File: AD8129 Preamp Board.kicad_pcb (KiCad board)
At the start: 2 copper layers, 50 x 42 mm, 39 parts, among them J1 ANT, J2 TUNE, J3 TRX, T1 Transformer_1P_1S, U1 AD8129, U2 L78L06_SO8

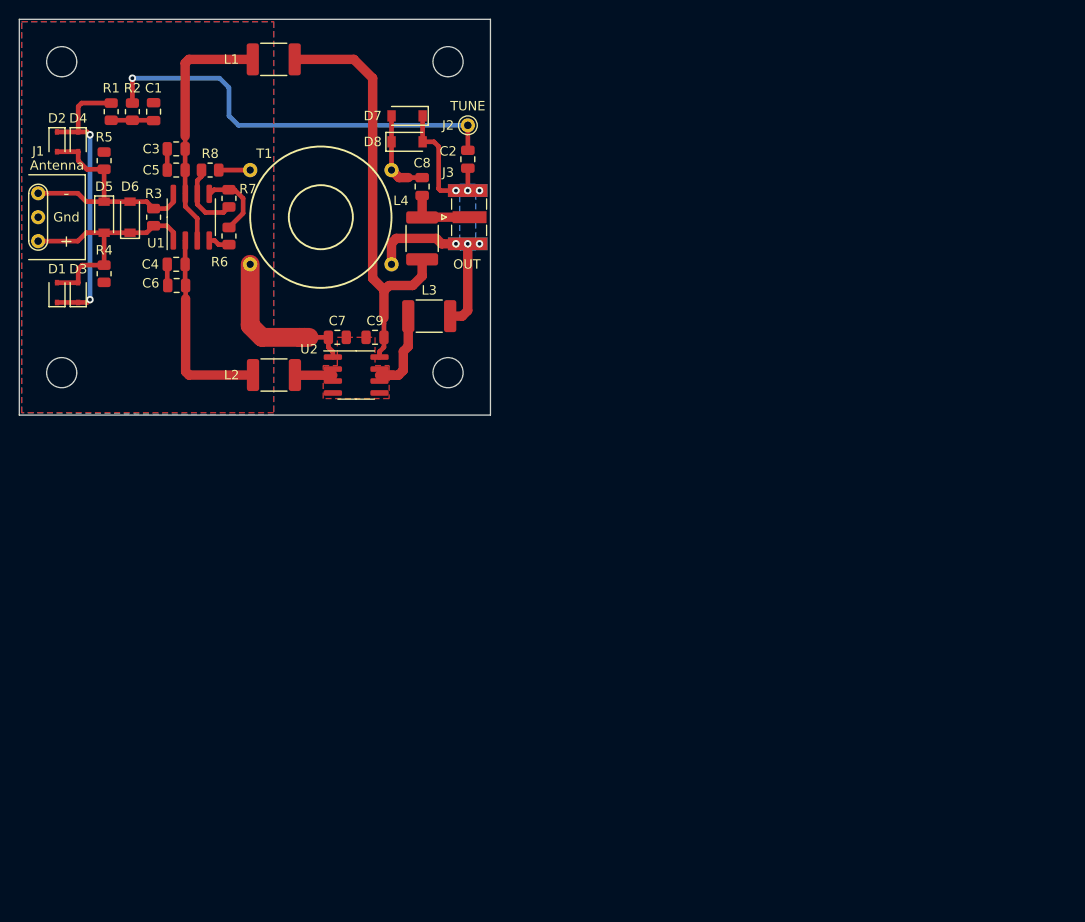
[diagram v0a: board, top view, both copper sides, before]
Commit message: FIX: board position
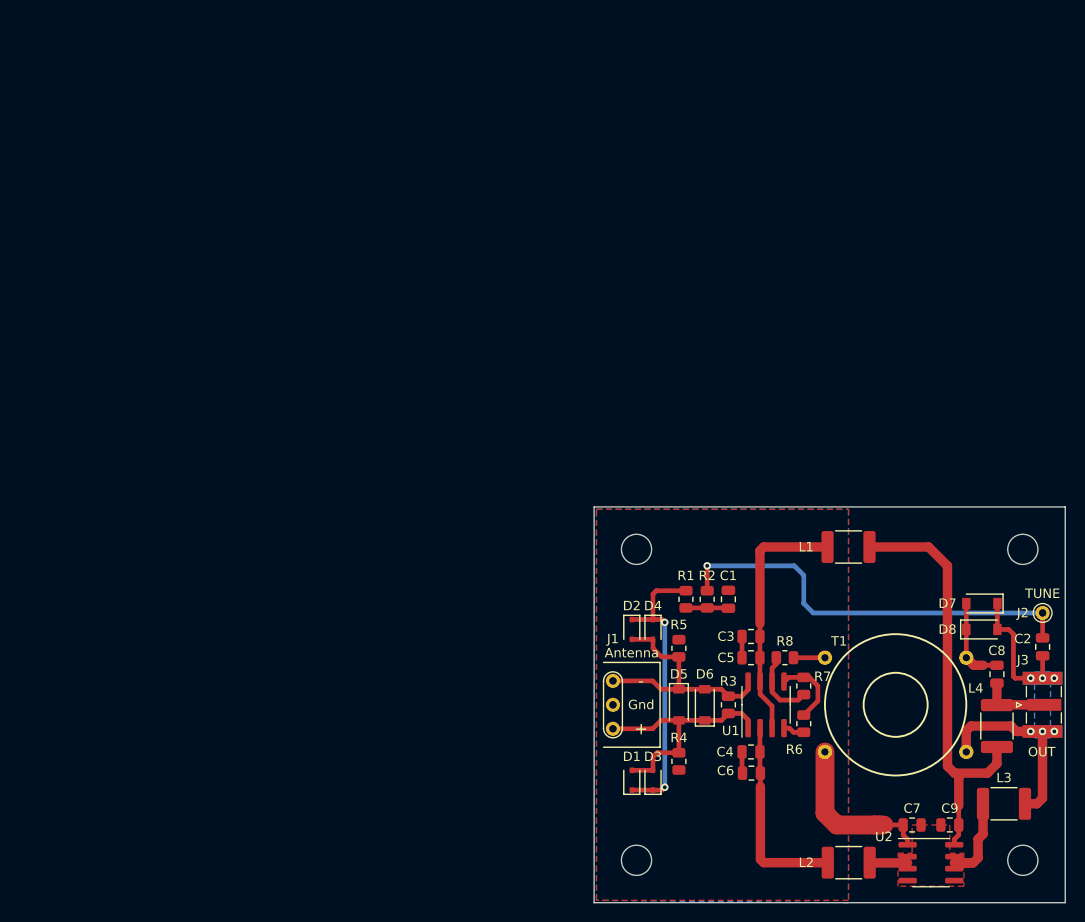
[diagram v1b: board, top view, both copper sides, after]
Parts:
- moved C1 80.0 mm to (135.2, 90.5)
- moved C2 80.0 mm to (168.6, 95.6)
- moved C3 80.0 mm to (137.7, 94.5)
- moved C4 80.0 mm to (137.7, 106.8)
- moved C5 80.0 mm to (137.7, 96.8)
- moved C6 80.0 mm to (137.7, 109.0)
- moved C7 80.0 mm to (154.8, 114.5)
- moved C8 80.0 mm to (163.8, 98.5)
- moved C9 80.0 mm to (158.8, 114.5)
- moved D1 80.0 mm to (125.0, 109.8)
- moved D2 80.0 mm to (125.0, 93.8)
- moved D3 80.0 mm to (127.2, 109.8)
- moved D4 80.0 mm to (127.2, 93.8)
- moved D5 80.0 mm to (130.0, 101.8)
- moved D6 80.0 mm to (132.8, 101.8)
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
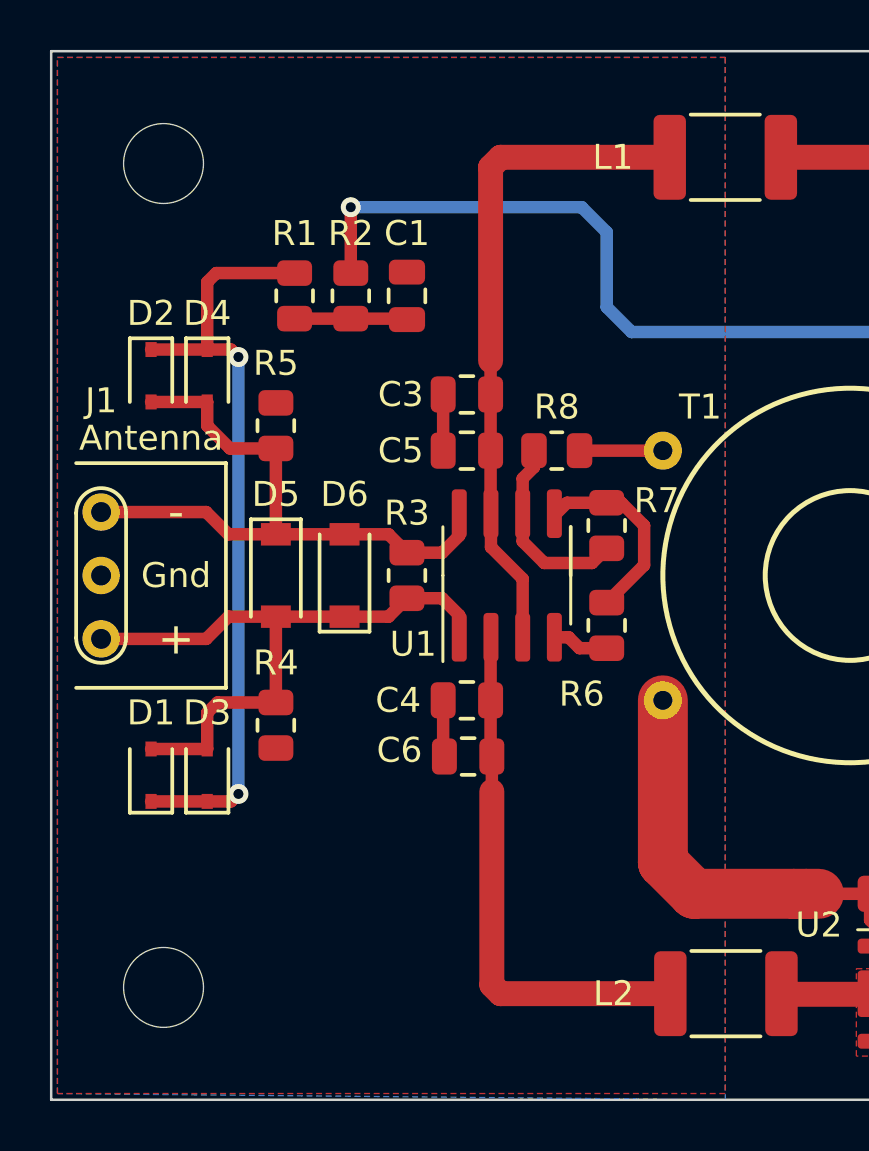
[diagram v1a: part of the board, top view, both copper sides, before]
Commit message: ADD: via stitching
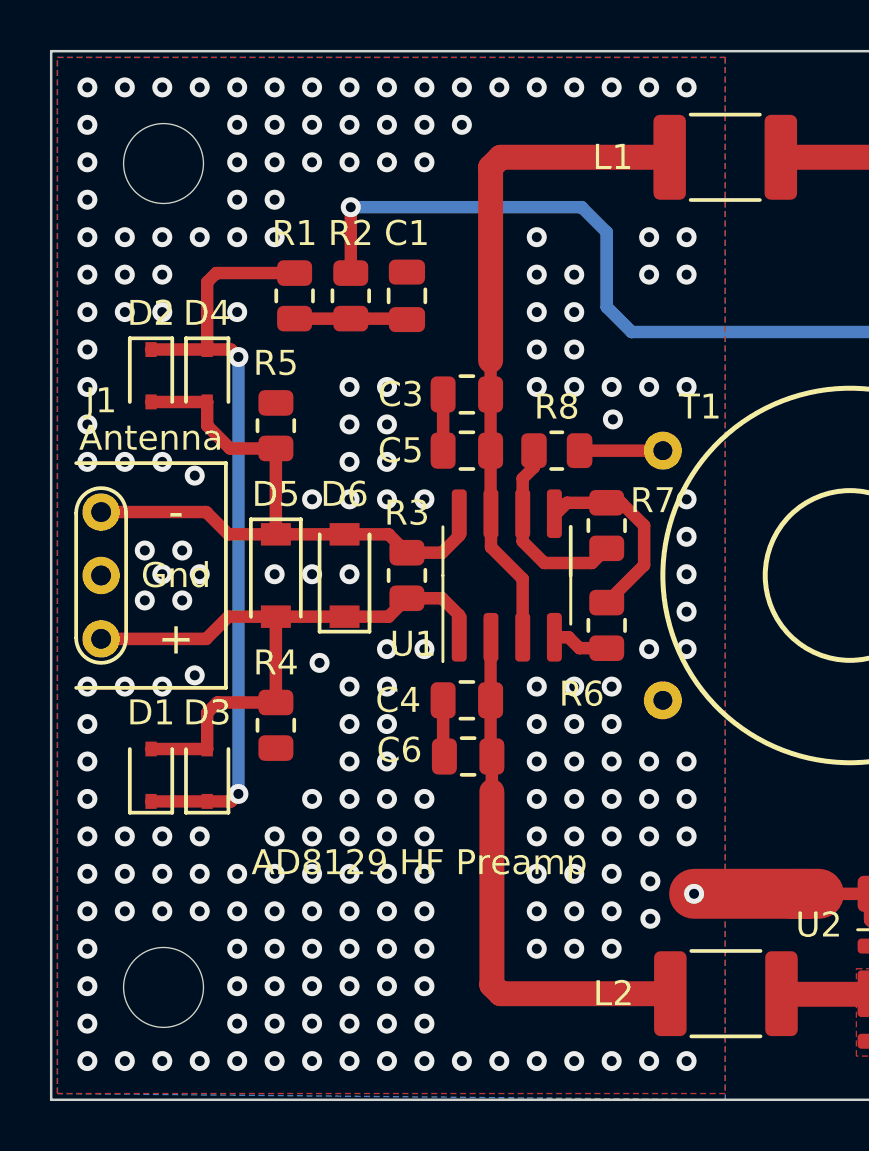
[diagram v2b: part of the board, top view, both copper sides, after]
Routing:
- net GND: track 24.4 -> 16.1 mm, vias 0 -> 217
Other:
- board text added: "AD8129 HF Preamp"

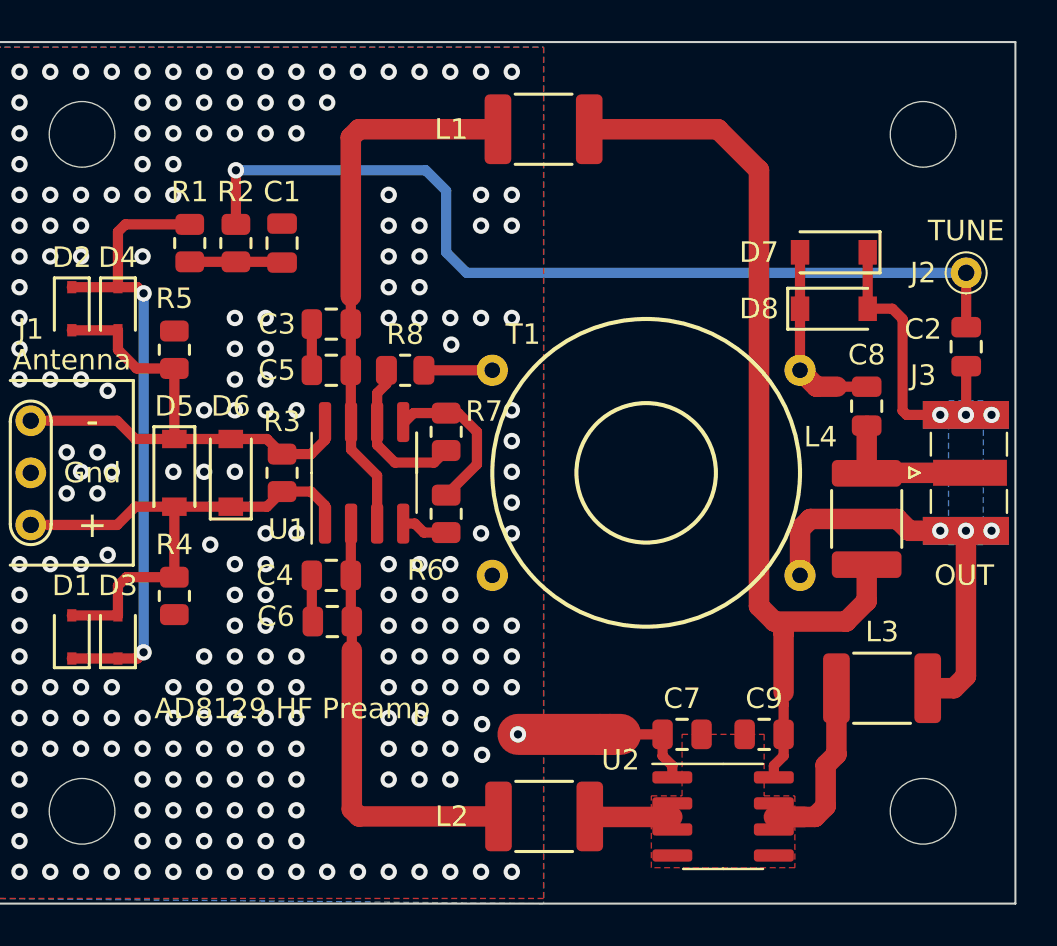
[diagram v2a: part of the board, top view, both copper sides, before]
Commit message: FIX: make burried vias, board info
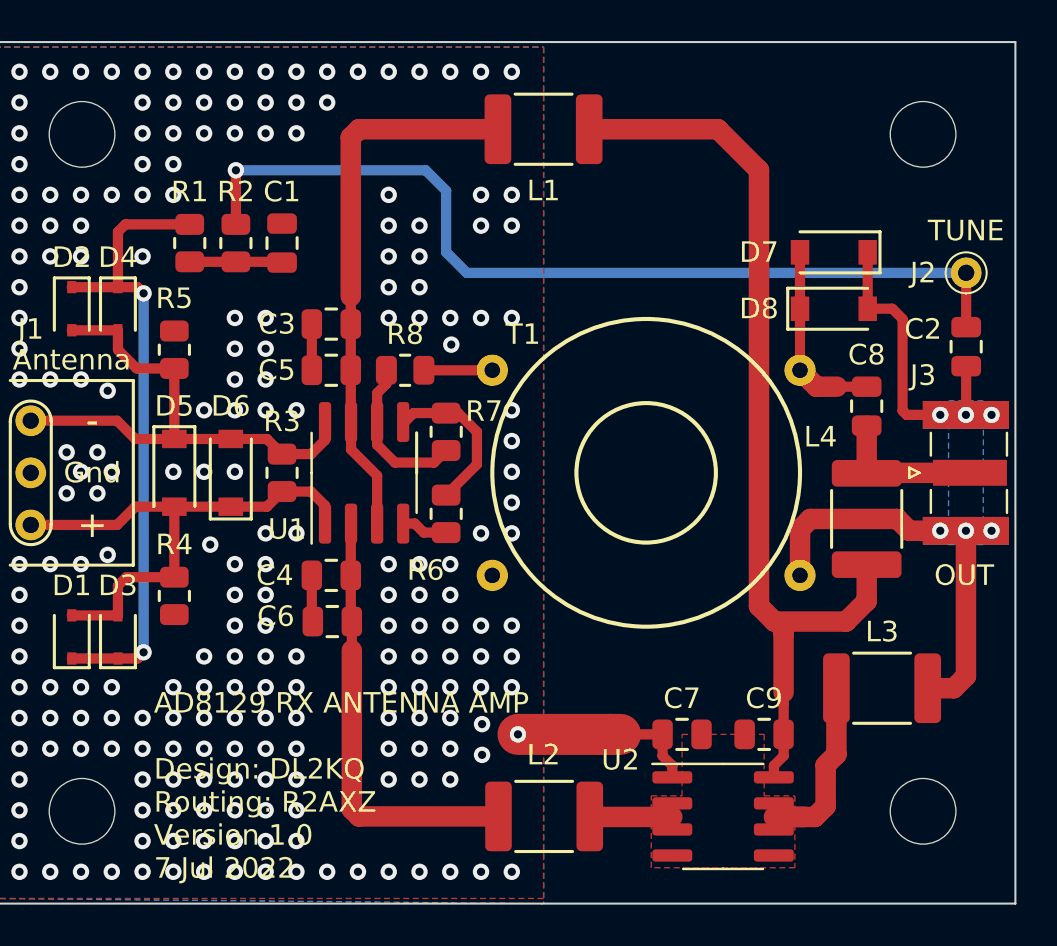
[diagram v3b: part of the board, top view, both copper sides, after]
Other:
- board text added: "AD8129 RX ANTENNA AMP Design: DL2KQ Routing: R2AXZ Version 1.0 7 Jul 2022"
- board text removed: "AD8129 HF Preamp"

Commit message: ADD: v1 final touch
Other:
- board text added: "Check out schematics for the input stage options."
- board text added: "Gain = 1 + R7/R6 Adjust R4, R5 for a desired Q, match within 0.1%."
- board text added: "Match R3 to the antenna impedance."
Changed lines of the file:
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@@
     (property "Sheetname" "")
     (attr smd)
-    (fp_text reference "L1" (at 0 3 180) (layer "F.SilkS")
+    (fp_text reference "L1" (at -4.25 1 180) (layer "F.SilkS")
       (effects (font (size 1 1) (thickness 0.15)))
     )
@@
     (property "Sheetname" "")
     (attr smd)
-    (fp_text reference "L2" (at 0.025 3 180) (layer "F.SilkS")
+    (fp_text reference "L2" (at 4.275 1 180) (layer "F.SilkS")
       (effects (font (size 1 1) (thickness 0.15)))
     )
@@
     (effects (font (size 1 1) (thickness 0.2)))
   )
+  (gr_text "Check out schematics\nfor the input stage\noptions." (at 129.25 83.75) (layer "F.SilkS")
+    (effects (font (size 1 1) (thickness 0.2)) (justify left))
+  )
   (gr_text "Antenna" (at 125 96.25) (layer "F.SilkS")
     (effects (font (size 1 1) (thickness 0.15)))
   )
+  (gr_text "Gain = 1 + R7/R6\nAdjust R4, R5 for\na desired Q, match\nwithin 0.1%." (at 140.25 90.5) (layer "F.SilkS")
+    (effects (font (size 1 1) (thickness 0.2)) (justify left))
+  )
+  (gr_text "Match R3 to the antenna\nimpedance." (at 140.25 111) (layer "F.SilkS")
+    (effects (font (size 1 1) (thickness 0.2)) (justify left))
+  )
   (gr_text "+" (at 126 104.29) (layer "F.SilkS")
     (effects (font (size 1.27 1.27) (thickness 0.15)))
@@
     (effects (font (size 1 1) (thickness 0.2)))
   )
-  (gr_text "AD8129 RX ANTENNA AMP\n\nDesign: DL2KQ\nRouting: R2AXZ\nVersion 1.0\n7 Jul 2022" (at 129 117) (layer "F.SilkS")
+  (gr_text "AD8129 RX ANTENNA AMP\nDesign: DL2KQ\nRouting: R2AXZ\nVersion 1.0\n7 Jul 2022" (at 129 117.75) (layer "F.SilkS")
     (effects (font (size 1 1) (thickness 0.2)) (justify left))
   )

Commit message: FIX: another final touch
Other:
- board text added: "For ferrite rod antenna, install D1-D4,R1,R2,C1,C2. Frame antenna: R3"
- board text removed: "Check out schematics for the input stage options."
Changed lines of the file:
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@@
     (property "Sheetname" "")
     (attr smd)
-    (fp_text reference "L1" (at -4.25 1 180) (layer "F.SilkS")
+    (fp_text reference "L1" (at 4 0 180) (layer "F.SilkS")
       (effects (font (size 1 1) (thickness 0.15)))
     )
@@
     (property "Sheetname" "")
     (attr smd)
-    (fp_text reference "L2" (at 4.275 1 180) (layer "F.SilkS")
+    (fp_text reference "L2" (at -3.975 0 180) (layer "F.SilkS")
       (effects (font (size 1 1) (thickness 0.15)))
     )
@@
     (effects (font (size 1 1) (thickness 0.2)))
   )
-  (gr_text "Check out schematics\nfor the input stage\noptions." (at 129.25 83.75) (layer "F.SilkS")
+  (gr_text "For ferrite rod antenna, install\nD1-D4,R1,R2,C1,C2.\nFrame antenna: R3" (at 129 83.75) (layer "F.SilkS")
     (effects (font (size 1 1) (thickness 0.2)) (justify left))
   )

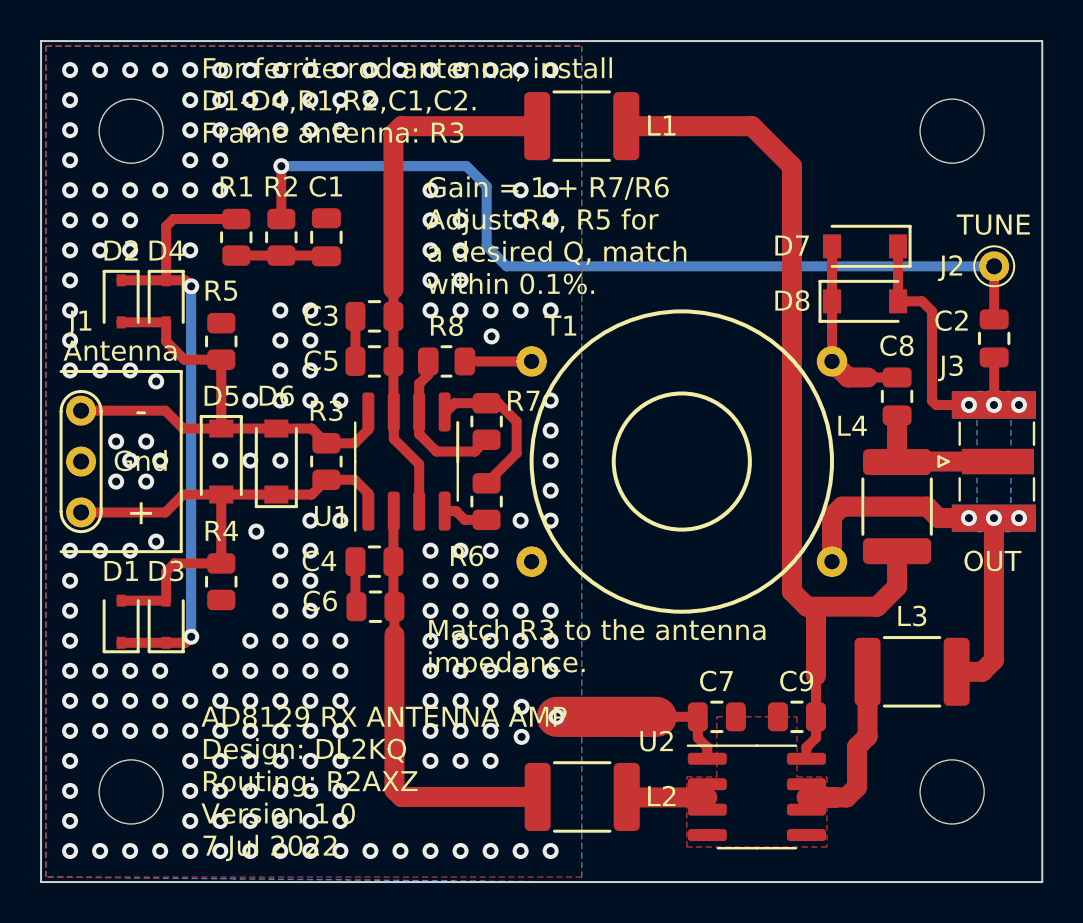
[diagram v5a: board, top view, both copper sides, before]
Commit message: ADD: capacitors, T1 shield
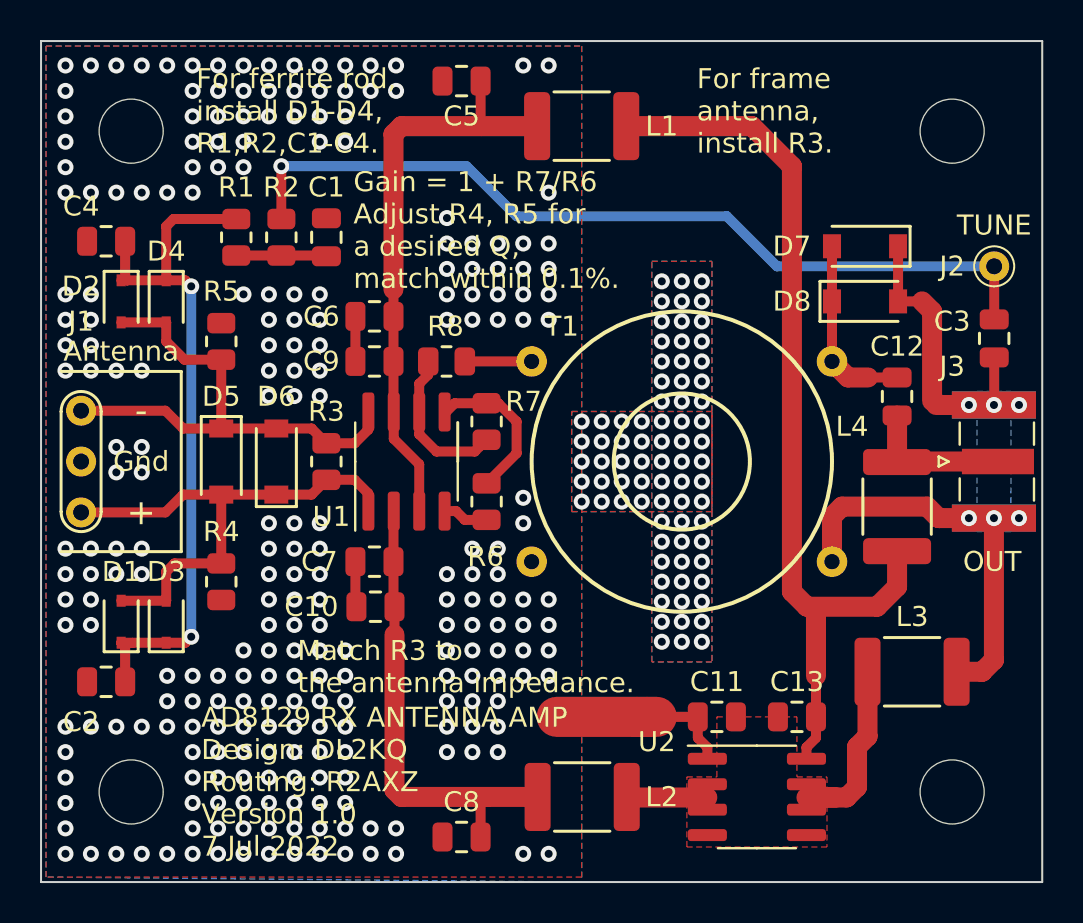
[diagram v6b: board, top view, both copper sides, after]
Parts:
- added C2: 100n, AD8129 Preamp Board:C_0805_2012Metric, F.Cu at (124.2, 112.8)
- added C4: 100n, AD8129 Preamp Board:C_0805_2012Metric, F.Cu at (124.2, 90.8)
- added C5: 100n, AD8129 Preamp Board:C_0805_2012Metric, F.Cu at (142.0, 82.8)
- added C8: 100n, AD8129 Preamp Board:C_0805_2012Metric, F.Cu at (142.0, 120.5)
- renumbered C6 to C10, C7 to C11, C8 to C12, C9 to C13, C2 to C3, C3 to C6, C4 to C7, C5 to C9
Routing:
- net Net-(C2-Pad1): track 31.1 -> 35.1 mm
- net Net-(C5-Pad2): track 26.7 -> 29.0 mm
- net Net-(C10-Pad2): track 21.2 -> 23.4 mm
- net TUNE: track 44.7 -> 43.0 mm
- net GND: vias 217 -> 325
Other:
- board text added: "For ferrite rod, install D1-D4, R1,R2,C1-С4."
- board text added: "For frame antenna, install R3."
- board text removed: "For ferrite rod antenna, install D1-D4,R1,R2,C1,C2. Frame antenna: R3"

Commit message: ADD: vias, fix DRC
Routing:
- net GND: vias 325 -> 347
